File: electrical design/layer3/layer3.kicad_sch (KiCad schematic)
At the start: 4 parts, among them J1 SH 1.0 6P, J2 SH 1.0 6P, J3 SH 1.0 6P, J4 SH 1.0 6P

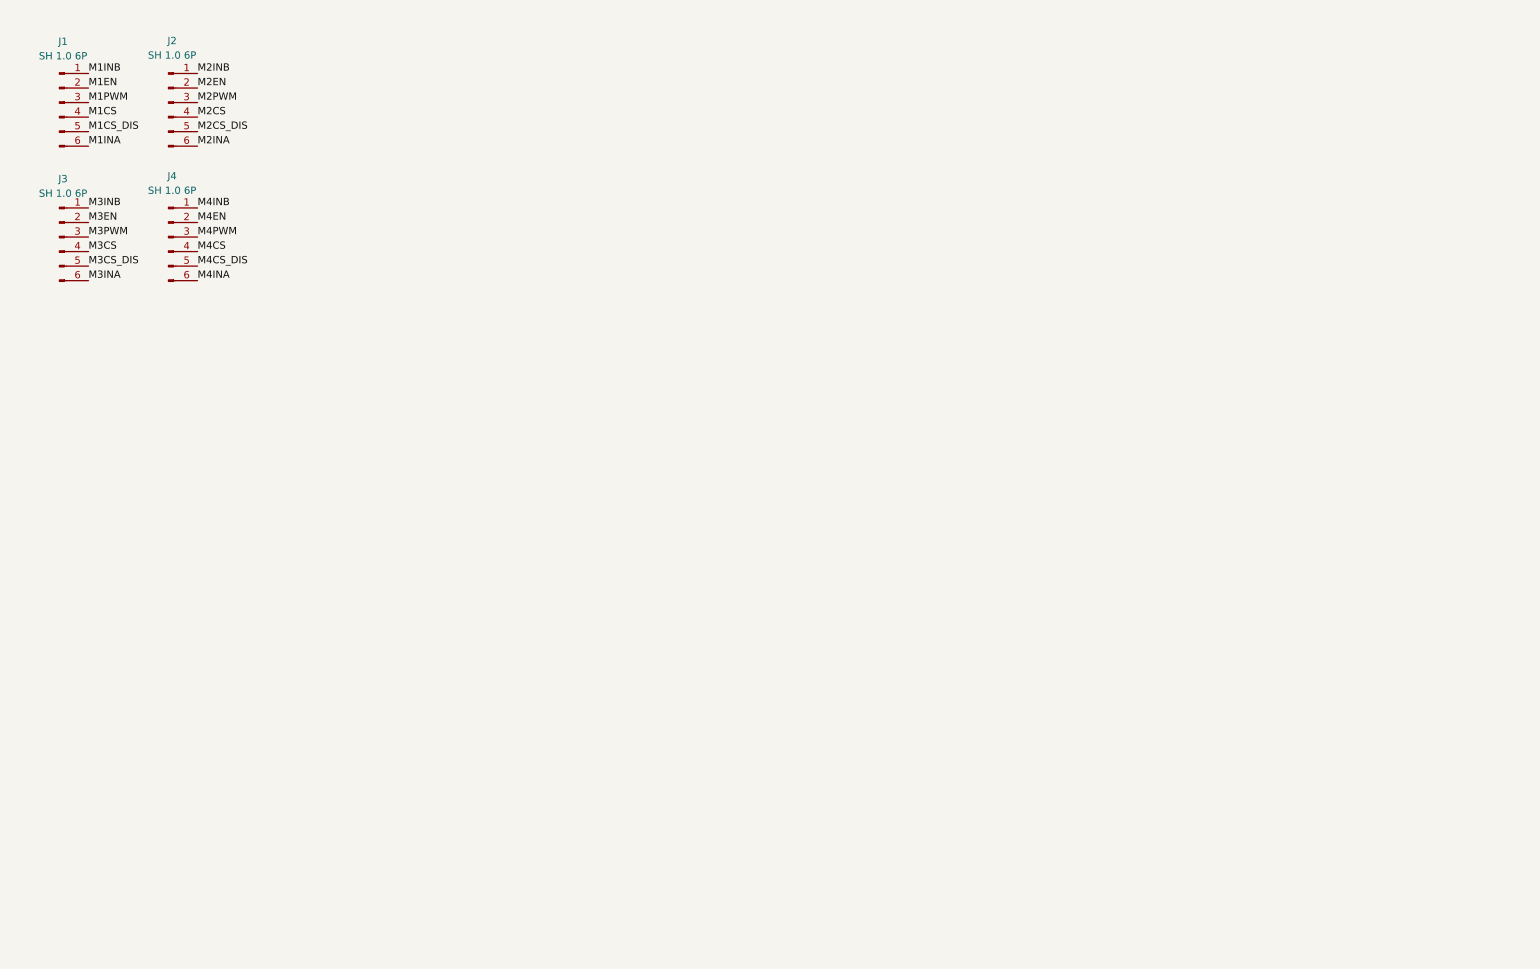
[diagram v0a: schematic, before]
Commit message: lay out components on l3
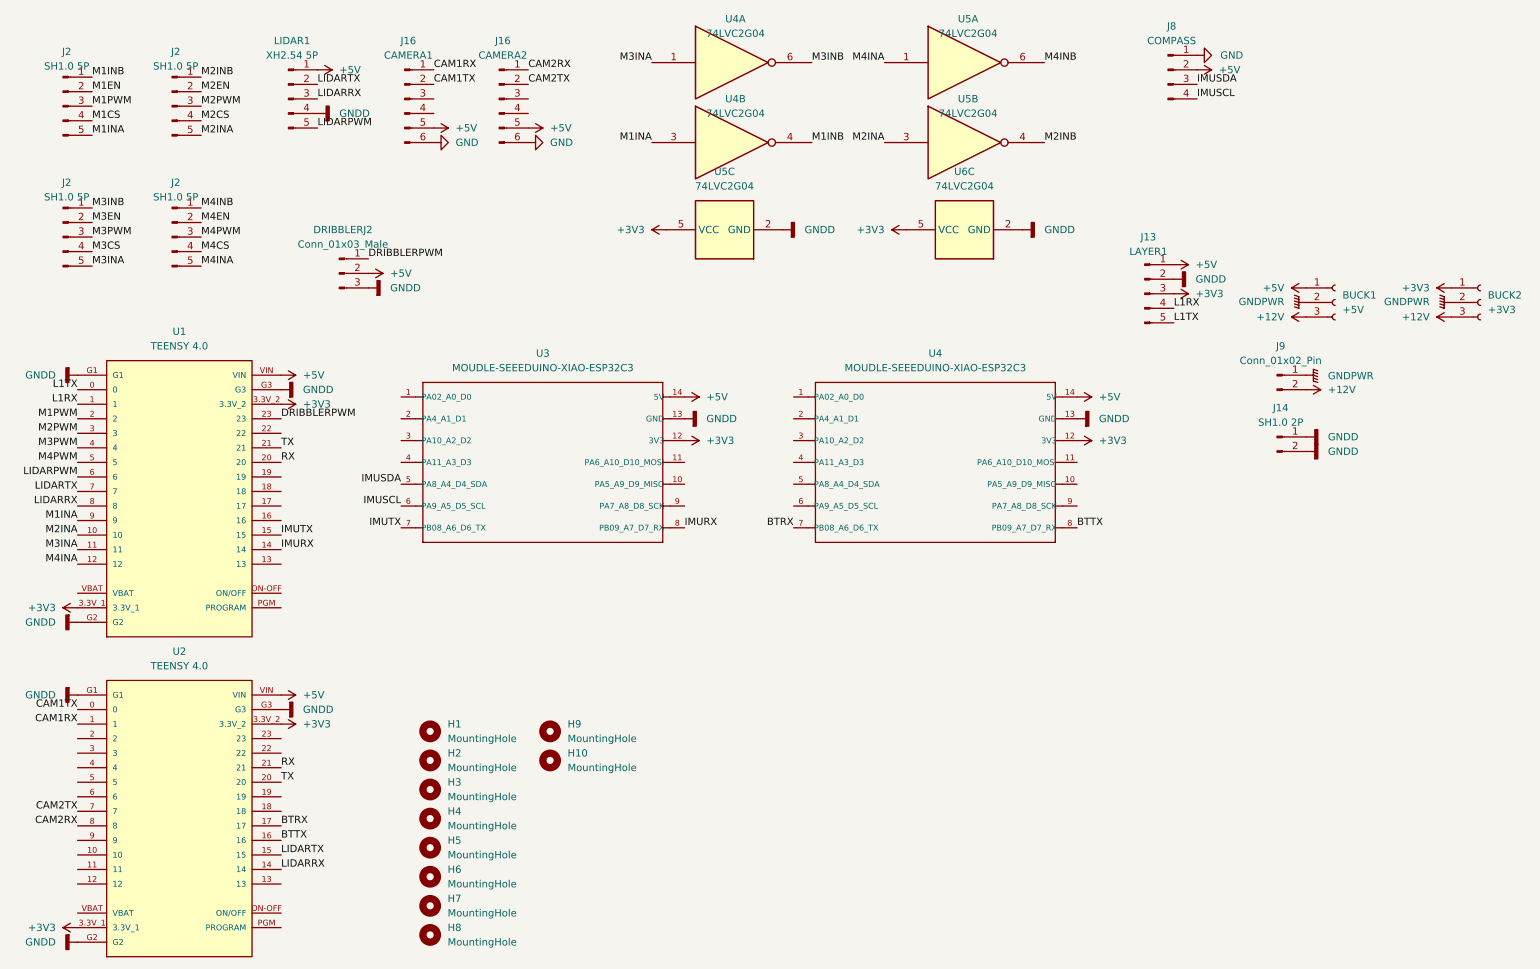
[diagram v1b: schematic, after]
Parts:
- removed J1, J2, J3, J4: SH 1.0 6P, Connector_JST:JST_SH_SM06B-SRSS-TB_1x06-1MP_P1.00mm_Horizontal, symbol Connector:Conn_01x06_Male
- added BUCK1: +5V, Connector_PinSocket_2.54mm:PinSocket_1x03_P2.54mm_Vertical, symbol Connector:Conn_01x03_Female
- added BUCK2: +3V3, Connector_PinSocket_2.54mm:PinSocket_1x03_P2.54mm_Vertical, symbol Connector:Conn_01x03_Female
- added DRIBBLERJ2: Conn_01x03_Male, Connector_PinHeader_2.54mm:PinHeader_1x03_P2.54mm_Vertical, symbol Connector:Conn_01x03_Male
- added H1, H10, H2, H3, H4, H5, H6, H7, H8, H9: MountingHole, MountingHole:MountingHole_3.2mm_M3_Pad, symbol Mechanical:MountingHole
- added J13: LAYER1, Connector_JST:JST_SH_SM05B-SRSS-TB_1x05-1MP_P1.00mm_Horizontal, symbol Connector:Conn_01x05_Pin
- added J14: SH1.0 2P, Connector_JST:JST_SH_SM02B-SRSS-TB_1x02-1MP_P1.00mm_Horizontal, symbol Connector:Conn_01x02_Pin
- added J16: CAMERA2, Connector_JST:JST_GH_BM06B-GHS-TBT_1x06-1MP_P1.25mm_Vertical, symbol Connector:Conn_01x06_Male
- added J16: CAMERA1, Connector_JST:JST_GH_BM06B-GHS-TBT_1x06-1MP_P1.25mm_Vertical, symbol Connector:Conn_01x06_Male
- added J2 (x4): SH1.0 5P, Connector_JST:JST_SH_SM05B-SRSS-TB_1x05-1MP_P1.00mm_Horizontal, symbol Connector:Conn_01x05_Pin
- added J8: COMPASS, Connector_JST:JST_SH_BM04B-SRSS-TB_1x04-1MP_P1.00mm_Vertical, symbol Connector:Conn_01x04_Pin
- added J9: Conn_01x02_Pin, Connector_JST:JST_XH_B2B-XH-A_1x02_P2.50mm_Vertical, symbol Connector:Conn_01x02_Pin
- added LIDAR1: XH2.54 5P, Connector_JST:JST_XH_B5B-XH-A_1x05_P2.50mm_Vertical, symbol Connector:Conn_01x05_Male
- added U1, U2: TEENSY 4.0, teensy:Teensy40, symbol DEV-15583:DEV-15583
- added U3: MOUDLE-SEEEDUINO-XIAO-ESP32C3, libraries:xiao-esp32c3, symbol MOUDLE-SEEEDUINO-XIAO-ESP32C3:MOUDLE-SEEEDUINO-XIAO-ESP32C3
- added U4, U5: 74LVC2G04, Package_TO_SOT_SMD:SOT-23-6, symbol 74xGxx:74LVC2G04
- added U6: 74LVC2G04, symbol 74xGxx:74LVC2G04
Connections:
- net M1CS: now also J2.4 (Pin_4)
- net M1EN: now also J2.2 (Pin_2)
- net M1INA: now also J2.5 (Pin_5), U1.9, U4.3
- net M1INB: now also J2.1 (Pin_1), U4.4
- net M1PWM: now also J2.3 (Pin_3), U1.2
- net M2CS: now also J2.4 (Pin_4)
- net M2EN: now also J2.2 (Pin_2)
- net M2INA: now also J2.5 (Pin_5), U1.10, U5.3
- net M2INB: now also J2.1 (Pin_1), U5.4
- net M2PWM: now also J2.3 (Pin_3), U1.3
- net M3CS: now also J2.4 (Pin_4)
- net M3EN: now also J2.2 (Pin_2)
- net M3INA: now also J2.5 (Pin_5), U1.11, U4.1
- net M3INB: now also J2.1 (Pin_1), U4.6
- net M3PWM: now also J2.3 (Pin_3), U1.4
- net M4CS: now also J2.4 (Pin_4)
- net M4EN: now also J2.2 (Pin_2)
- net M4INA: now also J2.5 (Pin_5), U1.12, U5.1
- net M4INB: now also J2.1 (Pin_1), U5.6
- net M4PWM: now also J2.3 (Pin_3), U1.5
- new net +12V: BUCK1.3 (Pin_3), BUCK2.3 (Pin_3), J9.2 (Pin_2)
- new net +3V3: BUCK2.1 (Pin_1), J13.3 (Pin_3), U1.3.3V_1, U1.3.3V_2, U2.3.3V_1, U2.3.3V_2, U3.12 (3V3), U4.12 (3V3), U5.5 (VCC), U6.5 (VCC)
- new net +5V: BUCK1.1 (Pin_1), DRIBBLERJ2.2 (Pin_2), J13.1 (Pin_1), J16.5 (Pin_5), J16.5 (Pin_5), J8.2 (Pin_2), LIDAR1.1 (Pin_1), U1.VIN, U2.VIN, U3.14 (5V), U4.14 (5V)
- new net BTRX: U2.17, U4.7 (PB08_A6_D6_TX)
- new net BTTX: U2.16, U4.8 (PB09_A7_D7_RX)
- new net CAM1RX: J16.1 (Pin_1), U2.1
- new net CAM1TX: J16.2 (Pin_2), U2.0
- new net CAM2RX: J16.1 (Pin_1), U2.8
- new net CAM2TX: J16.2 (Pin_2), U2.7
- new net DRIBBLERPWM: DRIBBLERJ2.1 (Pin_1), U1.23
- new net GND: J16.6 (Pin_6), J16.6 (Pin_6), J8.1 (Pin_1)
- new net GNDD: DRIBBLERJ2.3 (Pin_3), J13.2 (Pin_2), J14.1 (Pin_1), J14.2 (Pin_2), LIDAR1.4 (Pin_4), U1.G1, U1.G2, U1.G3, U2.G1, U2.G2, U2.G3, U3.13 (GND), U4.13 (GND), U5.2 (GND), U6.2 (GND)
- new net GNDPWR: BUCK1.2 (Pin_2), BUCK2.2 (Pin_2), J9.1 (Pin_1)
- new net IMURX: U1.14, U3.8 (PB09_A7_D7_RX)
- new net IMUSCL: J8.4 (Pin_4), U3.6 (PA9_A5_D5_SCL)
- new net IMUSDA: J8.3 (Pin_3), U3.5 (PA8_A4_D4_SDA)
- new net IMUTX: U1.15, U3.7 (PB08_A6_D6_TX)
- new net L1RX: J13.4 (Pin_4), U1.1
- new net L1TX: J13.5 (Pin_5), U1.0
- new net LIDARPWM: LIDAR1.5 (Pin_5), U1.6
- new net LIDARRX: LIDAR1.3 (Pin_3), U1.8, U2.14
- new net LIDARTX: LIDAR1.2 (Pin_2), U1.7, U2.15
- new net RX: U1.20, U2.21
- new net TX: U1.21, U2.20
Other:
- company: 8076ducc Robotics Competition Team -> ducc. Robotics

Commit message: update pcbs and mech drawings
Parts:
- added SW1: SW_DPDT_x2, Switches:SWITCH_SPDT_PTH_11.6X4.0MM_LOCK, symbol Switch:SW_DPDT_x2
- BUCK2: value +3V3 -> +5V
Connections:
- net M2EN is gone; now on net EN: J2.2 (Pin_2)
- net M3EN is gone; now on net EN: J2.2 (Pin_2)
- net M4EN is gone; now on net EN: J2.2 (Pin_2)
- net +3V3: now also SW1.1 (A); no longer BUCK2.1 (Pin_1)
- net +5V: now also BUCK2.1 (Pin_1); no longer J16.5 (Pin_5), J16.5 (Pin_5)
- net GNDD: now also J8.1 (Pin_1)
- net M1CS: now also U1.16
- net M1INA: now also U4.1; no longer U4.3
- net M1INB: now also U4.6; no longer U4.4
- net M2CS: now also U1.17
- net M2INA: now also U5.1; no longer U5.3
- net M2INB: now also U5.6; no longer U5.4
- net M3CS: now also U1.18
- net M3INA: now also U4.3; no longer U4.1
- net M3INB: now also U4.4; no longer U4.6
- net M4CS: now also U1.19
- net M4INA: now also U5.3; no longer U5.1
- net M4INB: now also U5.4; no longer U5.6
- removed net GND: J16.6 (Pin_6), J16.6 (Pin_6), J8.1 (Pin_1)
- net M1EN renamed EN
- net EN: now also SW1.2 (B)

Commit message: update pcbs for dual camera design
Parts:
- added J12: XH2.54 2P, Connector_JST:JST_XH_B2B-XH-A_1x02_P2.50mm_Vertical, symbol Connector:Conn_01x02_Pin
- added R1, R2, R3, R4, R5: 10k, Resistor_SMD:R_0603_1608Metric, symbol Device:R
- added R6, R7: R, Resistor_SMD:R_0603_1608Metric, symbol Device:R
- added SW2: SW_DIP_x05, Button_Switch_SMD:SW_DIP_SPSTx05_Slide_6.7x14.26mm_W8.61mm_P2.54mm_LowProfile, symbol Switch:SW_DIP_x05
- J9: value Conn_01x02_Pin -> XH2.54 2P
- U6: footprint (none) -> Package_TO_SOT_SMD:SOT-23-6
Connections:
- net +3V3: now also R1.1, R2.1, R3.1, R4.1, R5.1
- net +5V: now also J12.2 (Pin_2)
- net GNDD: now also SW2.1, SW2.2, SW2.3, SW2.4, SW2.5
- net GNDPWR: now also J12.1 (Pin_1)
- net IMUSCL: now also R7.1
- net IMUSDA: now also R6.1
- net STRAT1: now reaches U2.2
- net STRAT1: now also R1.2, SW2.10
- net STRAT2: now reaches U2.3
- net STRAT2: now also R2.2, SW2.9
- net STRAT3: now reaches U2.4
- net STRAT3: now also R3.2, SW2.8
- net STRAT4: now reaches U2.5
- net STRAT4: now also R4.2, SW2.7
- net STRAT5: now reaches U2.6
- net STRAT5: now also R5.2, SW2.6
- new net: R6.2, R7.2

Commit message: change EN switch to larger one
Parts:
- removed SW1: SW_DPDT_x2, Switches:SWITCH_SPDT_PTH_11.6X4.0MM_LOCK, symbol Switch:SW_DPDT_x2
- removed SW2: SW_DIP_x05, Button_Switch_SMD:SW_DIP_SPSTx05_Slide_6.7x14.26mm_W8.61mm_P2.54mm_LowProfile, symbol Switch:SW_DIP_x05
- added SW1: SW_SPDT, Switches:SWITCH_SPDT_PTH_12.7X6.7MM, symbol Switch:SW_SPDT
- added SW2: SW_DIP_x04, Button_Switch_SMD:SW_DIP_SPSTx04_Slide_6.7x11.72mm_W8.61mm_P2.54mm_LowProfile, symbol Switch:SW_DIP_x04
- J12: footprint Connector_JST:JST_XH_B2B-XH-A_1x02_P2.50mm_Vertical -> Connector_Wire:SolderWire-0.5sqmm_1x02_P4.6mm_D0.9mm_OD2.1mm
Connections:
- net +3V3: now also SW1.1 (A); no longer R5.1
- net +5V: no longer DRIBBLERJ2.2 (Pin_2)
- net EN: now also R5.2, SW1.2 (B)
- net GNDD: now also R5.1, SW2.1, SW2.2, SW2.3, SW2.4
- net STRAT1: now also SW2.8
- net STRAT2: now also SW2.7
- net STRAT3: now also SW2.6
- net STRAT4: now also SW2.5
- net STRAT5: no longer names the net of U2.6
- net STRAT5: no longer R5.2

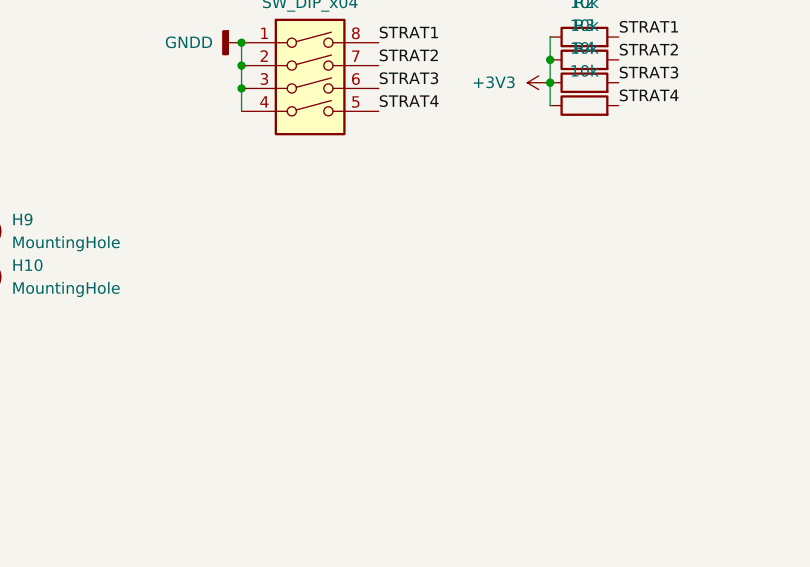
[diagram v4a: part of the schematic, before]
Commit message: add 5v test point on l3
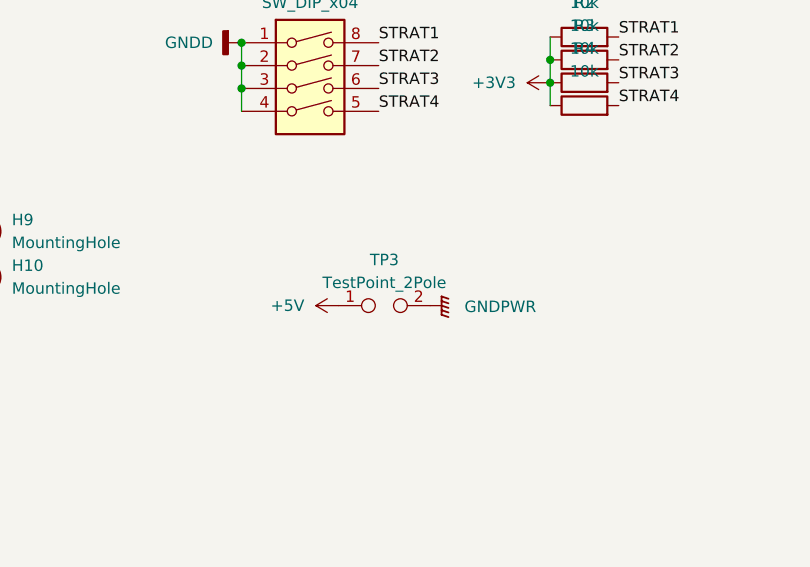
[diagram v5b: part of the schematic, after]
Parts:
- added TP3: TestPoint_2Pole, TestPoint:TestPoint_2Pads_Pitch2.54mm_Drill0.8mm, symbol Connector:TestPoint_2Pole
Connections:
- net +5V: now also TP3.1
- net GNDPWR: now also TP3.2
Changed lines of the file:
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@@
+    )
+  )
+  (symbol (lib_name "+5V_4") (lib_id "power:+5V") (at 151.13 153.035 90) (unit 1)
+    (in_bom yes) (on_board yes) (dnp no) (fields_autoplaced)
+    (property "Reference" "#PWR038" (at 154.94 153.035 0)
+      (effects (font (size 1.27 1.27)) hide)
+    )
+    (property "Value" "+5V" (at 147.32 153.035 90)
+      (effects (font (size 1.27 1.27)) (justify left))
+    )
+    (property "Footprint" "" (at 151.13 153.035 0)
+      (effects (font (size 1.27 1.27)) hide)
+    )
+    (property "Datasheet" "" (at 151.13 153.035 0)
+      (effects (font (size 1.27 1.27)) hide)
+    )
+    (pin "1")
+    (instances
+      (project "layer3"
+        (path "/e63e39d7-6ac0-4ffd-8aa3-1841a4541b55"
+          (reference "#PWR038") (unit 1)
+        )
+      )
     )
   )
@@
         (path "/e63e39d7-6ac0-4ffd-8aa3-1841a4541b55"
           (reference "#PWR044") (unit 1)
+        )
+      )
+    )
+  )
+  (symbol (lib_id "power:GNDPWR") (at 161.29 153.035 90) (unit 1)
+    (in_bom yes) (on_board yes) (dnp no) (fields_autoplaced)
+    (property "Reference" "#PWR033" (at 166.37 153.035 0)
+      (effects (font (size 1.27 1.27)) hide)
+    )
+    (property "Value" "GNDPWR" (at 165.1 153.162 90)
+      (effects (font (size 1.27 1.27)) (justify right))
+    )
+    (property "Footprint" "" (at 162.56 153.035 0)
+      (effects (font (size 1.27 1.27)) hide)
+    )
+    (property "Datasheet" "" (at 162.56 153.035 0)
+      (effects (font (size 1.27 1.27)) hide)
+    )
+    (pin "1")
+    (instances
+      (project "layer1"
+        (path "/32d54464-fd6f-441d-9cef-d3e4fabf9fe1"
+          (reference "#PWR033") (unit 1)
+        )
+      )
+      (project "layer3"
+        (path "/e63e39d7-6ac0-4ffd-8aa3-1841a4541b55"
+          (reference "#PWR047") (unit 1)
         )
       )
@@
         )
       )
+    )
+  )
+  (symbol (lib_id "Connector:TestPoint_2Pole") (at 156.21 153.035 0) (unit 1)
+    (in_bom yes) (on_board yes) (dnp no) (fields_autoplaced)
+    (property "Reference" "TP3" (at 156.21 147.955 0)
+      (effects (font (size 1.27 1.27)))
+    )
+    (property "Value" "TestPoint_2Pole" (at 156.21 150.495 0)
+      (effects (font (size 1.27 1.27)))
+    )
+    (property "Footprint" "TestPoint:TestPoint_2Pads_Pitch2.54mm_Drill0.8mm" (at 156.21 153.035 0)
+      (effects (font (size 1.27 1.27)) hide)
+    )
+    (property "Datasheet" "~" (at 156.21 153.035 0)
+      (effects (font (size 1.27 1.27)) hide)
+    )
+    (pin "1")
+    (pin "2")
+    (instances
+      (project "layer1"
+        (path "/32d54464-fd6f-441d-9cef-d3e4fabf9fe1"
+          (reference "TP3") (unit 1)
+        )
+      )
+      (project "layer3"
+        (path "/e63e39d7-6ac0-4ffd-8aa3-1841a4541b55"
+          (reference "TP1") (unit 1)
+        )
+      )
